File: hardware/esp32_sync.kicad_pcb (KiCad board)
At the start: 2 copper layers, 127 x 101.6 mm, 279 parts, among them J11 USB_B_Micro, J12 Barrel_Jack, J2 Conn_01x02_Male, J21 GPIO, J22 I2S, J24 AUX0, J25 AUX1, J31 IDC SER, J32 SER1, J33 IDC SER, J34 SER2, J42 DS_3.3V, J43 DS0_EXT, J44 DS1_EXT, J45 DS2_EXT, J46 DS3_EXT, J51 AV, J52 AS0_EXT, J53 AS1_EXT, Q11 S8050, Q12 S8050, Q41 S8050, Q42 S8050, Q43 S8050, SW2 RESET, U1 CP2104, U11 SRV05-4, U13 AMS1117-3.3, U2 ESP32-WROOM-32D, U3 SP3232, U41 74AHC04, U42 74HC595, U43 74HC595, U45 TC4427, U46 TC4427, U51 DAC8562SDGSR, U52 NE5532, U53 NE5532

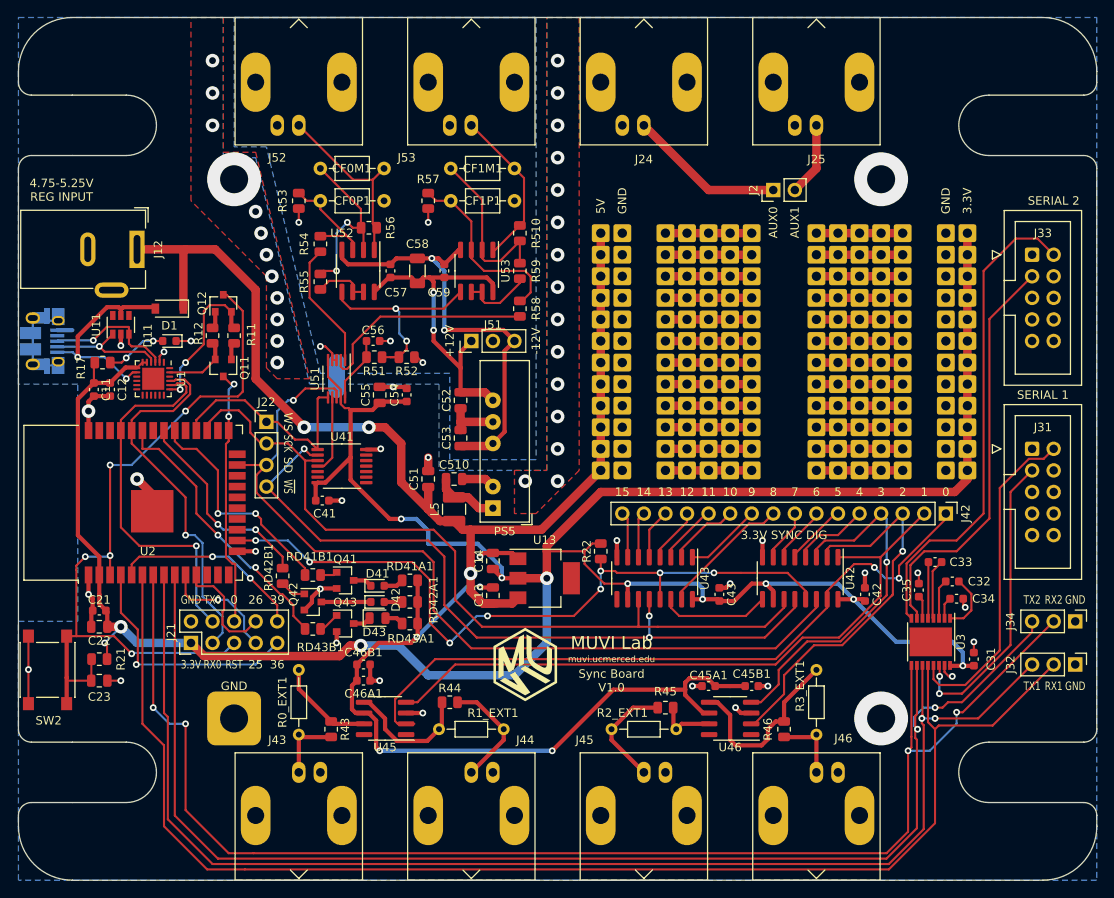
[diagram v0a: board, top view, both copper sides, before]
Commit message: Modified firmware for hardware, rev. 2 of PCB.
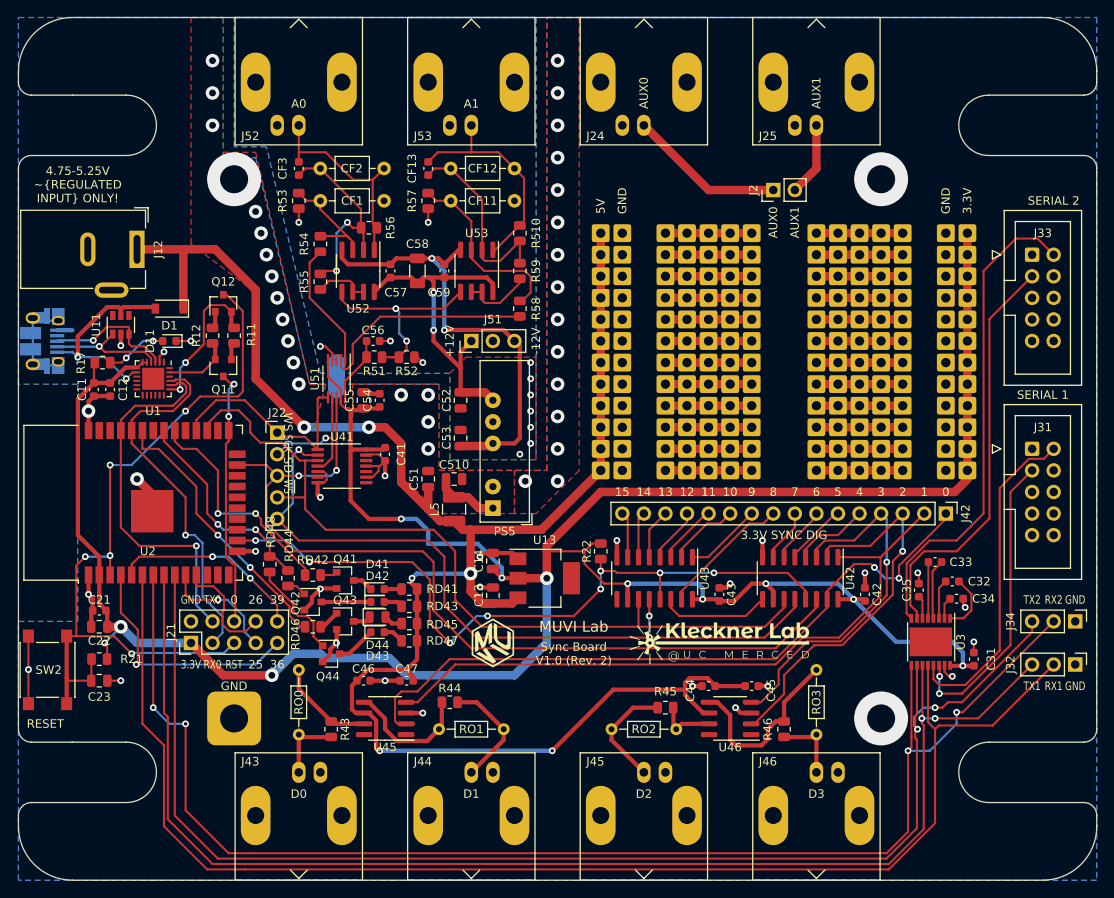
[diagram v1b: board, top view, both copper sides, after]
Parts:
- removed R1_EXT1: -, Resistor_THT:R_Axial_DIN0204_L3.6mm_D1.6mm_P7.62mm_Horizontal
- removed RD43A1: 100, Resistor_SMD:R_0805_2012Metric
- removed RD43B1: 4.7K, Resistor_SMD:R_0805_2012Metric
- removed the svg2mod at (123.2, 139.7)
- removed the svg2mod at (147.3, 134.6)
- added ?: , Logos:kleckner_lab_p_10mm, B.Cu at (127.0, 141.0)
- added ?: , Logos:kleckner_lab_p_5mm, F.Cu at (146.1, 137.2)
- added CF13: 30PF/50V, Capacitor_SMD:C_0603_1608Metric, F.Cu at (111.8, 81.3)
- added CF3: 30PF/50V, Capacitor_SMD:C_0603_1608Metric, F.Cu at (96.5, 81.3)
- added D44: GREEN, LED_SMD:LED_0603_1608Metric, F.Cu at (105.8, 135.9)
- added Q44: S8050, Package_TO_SOT_SMD:SOT-23, F.Cu at (100.3, 138.4)
- added RD45: 100, Resistor_SMD:R_0805_2012Metric, F.Cu at (109.5, 134.9)
- added RD46: 4.7K, Resistor_SMD:R_0805_2012Metric, F.Cu at (98.2, 135.3)
- added RD47: 82, Resistor_SMD:R_0805_2012Metric, F.Cu at (109.5, 136.9)
- added RD48: 4.7K, Resistor_SMD:R_0805_2012Metric, F.Cu at (93.1, 127.9)
- added RO1: -, Resistor_THT:R_Axial_DIN0204_L3.6mm_D1.6mm_P7.62mm_Horizontal, F.Cu at (120.7, 147.3)
- added svg2mod: G***, Logos:muvi_5mm, F.Cu at (119.4, 137.2)
- added svg2mod: G***, Logos:muvi_10mm, B.Cu at (141.6, 129.5)
- J22: footprint Connector_PinHeader_2.54mm:PinHeader_1x04_P2.54mm_Vertical -> Connector_PinHeader_2.54mm:PinHeader_1x05_P2.54mm_Vertical
- moved C41 9.19 mm to (106.7, 114.9), turned to 270 degrees
- moved C47 5.43 mm to (109.2, 141.6), turned to 180 degrees
- moved C54 3.24 mm to (106.0, 108.6)
- moved C55 2.01 mm to (104.1, 108.6)
- moved J22 1.80 mm to (94.0, 112.4)
- moved RD41 1.02 mm to (109.5, 130.8)
- moved RD44 0.69 mm to (95.2, 129.5)
- moved RD43 0.51 mm to (109.5, 132.8)
- moved D41 0.38 mm to (105.8, 130.8)
- moved Q43 0.25 mm to (102.0, 134.6)
- moved D43 0.13 mm to (105.8, 134.1)
- renumbered C45A1 to C44, C45B1 to C45, C46A1 to C46, C46B1 to C47, CF0P1 to CF1, CF1P1 to CF11, CF1M1 to CF12, CF0M1 to CF2, RD41A1 to RD41, RD41B1 to RD42, RD42A1 to RD43, RD42B1 to RD44, R0_EXT1 to RO0, R2_EXT1 to RO2, R3_EXT1 to RO3
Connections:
- J22 pad 2: /I2S_SCK -> /~I2S_SCK
- J22 pad 4: /DS_STCP -> /I2S_SCK
- U41 pad 11: (no net) -> GND
- U41 pad 13: (no net) -> GND
- U41 pad 14: GND -> /VDD33
- U41 pad 4: Net-(U41-Pad4) -> /~I2S_SCK
- U41 pad 5: (no net) -> GND
- U41 pad 7: /VDD33 -> GND
- U41 pad 9: (no net) -> GND
- U51 pad 7: Net-(U41-Pad4) -> /~I2S_SCK
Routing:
- net /~I2S_SCK: track 0.00 -> 16.6 mm, vias 0 -> 1
- net Net-(Q44-Pad1): track 0.00 -> 11.9 mm
- net Net-(U41-Pad4): track 9.23 -> 0.00 mm
- net /AS1_EXT: track 18.9 -> 26.3 mm
- net Net-(D44-Pad1): track 0.00 -> 4.73 mm
- net /VDD33: track 328.6 -> 324.8 mm
- net /I2S_SCK: track 94.0 -> 97.3 mm
- net /AS0_EXT: track 22.1 -> 25.1 mm
- net Net-(CF12-Pad1): track 20.2 -> 23.2 mm
- net Net-(CF2-Pad2): track 21.8 -> 24.7 mm
- net Net-(D44-Pad2): track 0.00 -> 2.47 mm
- net /VSS12: track 51.5 -> 53.5 mm
- net /I2S_SD: track 102.9 -> 104.4 mm, vias 1 -> 2
- net GND: track 100.7 -> 101.9 mm, vias 64 -> 74
- net /LED_G: track 24.2 -> 25.1 mm
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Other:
- board text added: "4.75-5.25V ~REGULATED INPUT ONLY!"
- board text added: "A0"
- board text added: "A1"
- board text added: "Anaglog/Digital Synchronizer Board Version 1.0 (PCB Rev. 2) Developed by the Kleckner and MUVI Labs at UC Merced faculty.ucmerced.edu/dkleckner muvi.ucmerced.edu"
- board text added: "D0"
- board text added: "D1"
- board text added: "D2"
- board text added: "D3"
- board text added: "RESET"
- board text added: "Sync Board V1.0 (Rev. 2)"
- board text removed: "4.75-5.25V REG INPUT"
- board text removed: "Anaglog/Digital Synchronizer Board Version 1.0 Developed by the Kleckner and MUVI Labs at UC Merced faculty.ucmerced.edu/dkleckner muvi.ucmerced.edu"
- board text removed: "Sync Board V1.0"
- board text removed: "muvi.ucmerced.edu"
